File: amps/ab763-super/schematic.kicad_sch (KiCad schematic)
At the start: 122 parts, among them T1 125P5D · 360-0-360V, T2 125C1A, T3 125A9A, T4 125A20B

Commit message: Fix: AB763 Super PI tail, feedback 100, recovery grid leak, reservoir pair and valve sections, as the C-FD drawings show them
- PI tail: the 22K lands on the feedback node, with the 820 from the speaker,
  the .1-200 from the cold grid and a 100 to ground (schematic sh-001 at
  3299 x 2551, crop s-pifb). The sheet grounded the tail and had no 100.
  New RFB1 on the sheet and in the BOM. netlist.cir now has RT2 JPI NFB,
  RFB1 NFB 0 100 and RNFB NFB 0 820, as the Twin models it. The PI plates
  and tail re-simulate to 255.8 / 249.3 V and 97.5 / 95.5 V; the notes'
  table follows.
- Board: RT2 stands on the top row from the tail junction to node F, and RFB1
  from node F to ground; the layout letters '100' at the board's top edge.
  The speaker anchor names SPK.tip, so the 820 is DC-checked. The tremolo
  parts the board placed under the old sheet's names are renamed to the
  drawn ladder's CTO2, CTO3 and RTOG2. The 27K bias leg's declaration is
  renamed RINT -> RBIAS2. The filter-can scope rule now covers C10-C13, the
  series pair its reason already names.
- RGR1 220K is the recovery grid's leak to ground, and the tank output lands
  on the grid (crop s-recov). The sheet drew it in series. sch_map maps the
  netlist's RGRV to it.
- The reservoir is two 70-350 cans in series, C10 over the new C13, each with
  its own 220K 1W across it (crop s-reservoir). The sheet lumped one 70 uF
  with both 220K to ground.
- V6 and V5 sections: the layout page (3299 x 2551 copy) runs the 82K to
  pin 1 and the 100K to pin 6, and puts the oscillator on 1/2/3 (+280 V pin
  1, +2.5 V pin 3) and the lamp driver on 6/7/8 (+390 V pin 6, +17.0 V pin 8).
  V6A, V5A are unit 2; V6B, V5B unit 1.
- netlist.cir: the dry node GDRY is modelled (RGD1, CBD1, CCV2, CRS), as on
  the Twin.

Co-Authored-By: Claude Opus 5 (1M context) <noreply@anthropic.com>
Claude-Session: https://claude.ai/code/session_01KBMfdh37HmCL2iWcBiL5J1
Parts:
- removed CBIAS: 25u 50V, symbol cx:C
- removed CCD1: .1u, symbol cx:C
- removed RT2: 22k, symbol cx:R
- removed RTO10: 10M, symbol cx:R
- removed RTOG1: 1M, symbol cx:R
- removed V5A: 12AX7, symbol cx:TRIODE
- removed V6B: 12AT7, symbol cx:TRIODE
- added C13: 70u 350V, symbol cx:C
- added RBIAS2: 27k, symbol cx:R
- added RFB1: 100, symbol cx:R
- added RGPA, RTOG2: 1M, symbol cx:R
- added RLPA: 82k 5%, symbol cx:R
- added RMIXV: 220k, symbol cx:R
- added T1: 125P5D · 360-0-360V, symbol cx:PT
- added VRSPD: 3M-RA speed, symbol cx:POT
- C10: value 70u -> 70u 350V
- CBIAS: renamed from RBIAS2; value 27k -> 25u 50V; symbol cx:R -> cx:C
- CCD1: renamed from RMIXV; value 220k -> .1u; symbol cx:R -> cx:C
- CKTO1: renamed from VRSPD; value 3M-RA speed -> 25u; symbol cx:POT -> cx:C
- RLAMP: renamed from T1; value 125P5D · 360-0-360V -> 100k; symbol cx:PT -> cx:R
- RT2: renamed from RGPA; value 1M -> 22k
- RTO10: renamed from RLAMP; value 100k -> 10M
- V5A: renamed from CKTO1; value 25u -> 12AX7; symbol cx:C -> cx:TRIODE; Basing_unit (none) -> 2
- V5B: Basing_unit (none) -> 1
- V6A: Basing_unit (none) -> 2
- V6B: renamed from RLPA; value 82k 5% -> 12AT7; symbol cx:R -> cx:TRIODE; Basing_unit (none) -> 1
- renumbered RTOG2 to RTOG1
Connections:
- net BC: now also RLPA.1; no longer V6B.1
- net BIAS FILTER: now also CBIAS.1
- net BP1: now also RLAMP.2, RTO10.1; no longer RTO10.2
- net GND: now also CKTO1.2, RGR1.2, C13.2, RBIAS2.2, RFB1.2, T1.4 (HT_CT); no longer C10.2, RBL1.2, RLAMP.4 (HT_CT), V5A.2
- net HT_A: now also T1.3 (HT_A); no longer RLAMP.3 (HT_A)
- net HT_B: now also T1.5 (HT_B); no longer RLAMP.5 (HT_B)
- net MAINS: now also T1.1 (PRI_1); no longer RLAMP.1 (PRI_1)
- net MAINS N: now also T1.2 (PRI_2); no longer RLAMP.2 (PRI_2)
- net PIG: now also RMIXV.2; no longer CCD1.2
- net TANK RET: now also V3B.2 (G)
- net at VRBIAS.3: now also RBIAS2.1; no longer CBIAS.1
- net at C2.1, RLPB.2: now also V6B.1 (P)
- net at CPIA.2, V6A.2 (G): now also RGPA.1; no longer RT2.1
- net at RGPB.1, RTAIL.1: now also RT2.1, RGPA.2; no longer RT2.2
- net at RTAIL.2, V6A.3 (K): now also V6B.3 (K)
- net at VRINT.1: now also CCD1.2, RMIXV.1; no longer CCD1.1
- net at CTO1.1, RTO2.2: now also V5A.1 (P)
- net at C10.1, RBL1.1, T2.1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: no longer RBL2.1
- net at OPTO.2 (L2): now also RLAMP.1; no longer RTO10.1
- net at CTO1.2, CTO2.2: now also VRSPD.1, VRSPD.2 (W); no longer CKTO1.1, CKTO1.2 (W)
- net at RTO1.1: now also VRSPD.3; no longer CKTO1.3
- net at RKTO1.1: now also CKTO1.1, V5A.3 (K); no longer V5A.1
- net at OPTO.1 (L1), V5B.1 (P): now also RTO10.2
- net at CTO2.1, CTO3.1, V5B.2 (G): now also RTOG1.2
- net at CPIB.1, RNFB.2: now also RT2.2, RFB1.1
- net at RTOG1.1, RTOG3.1: now also RTOG2.1
- net at C1.1, V6A.1 (P): now also RLPA.2; no longer V6B.2
- net at CPIB.2, RGPB.2: now also V6B.2 (G)
- net at CTO3.2: now also V5A.2 (G), RTOG2.2; no longer RTOG1.2
- net at RLD1.2, V3A.1 (P): now also CCD1.1
- new net: C10.2, C13.1, RBL1.2, RBL2.1
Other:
- moved on the sheet: RT2, RTO10, RTOG1

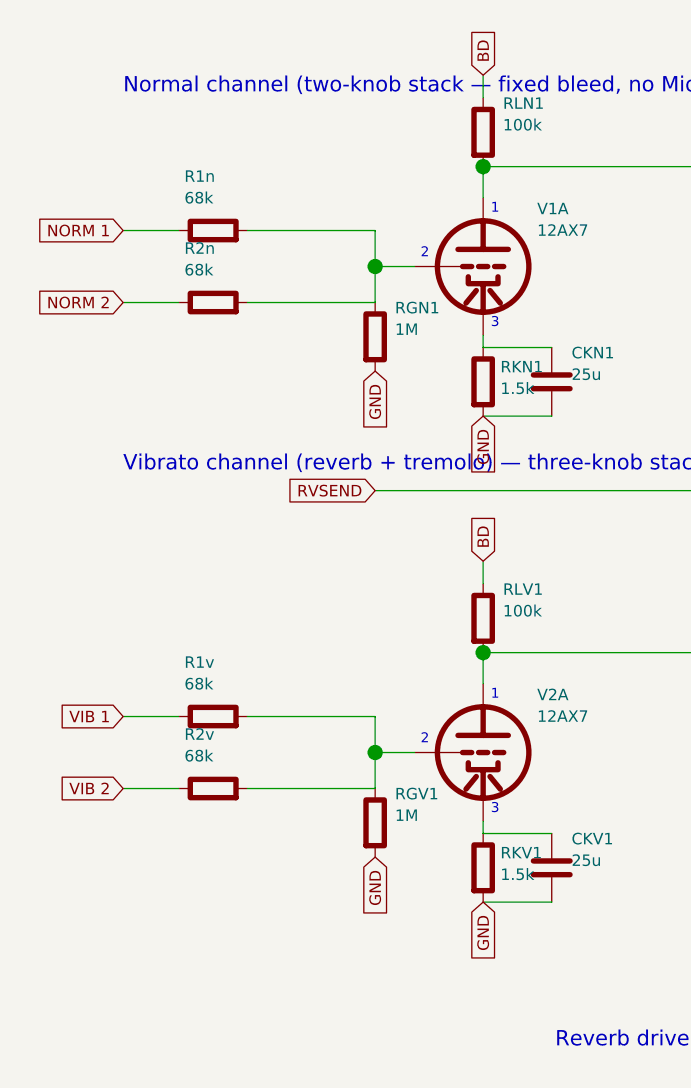
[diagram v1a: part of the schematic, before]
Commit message: AB763 Super (draft): input leaks at jack 1's tip (V1 audit carry-over)
The Super Reverb's own C-FD schematic (cached 2161x1500 capture, title
block 'SUPER-REVERB-AMP AB763', C-FD) hangs each channel's 1M from jack
1's tip, jack side of its lower 68k: Normal crop 90,250,300,500,
Vibrato 90,640,300,890. Jack 2's contact -> jack 1's tip, jack 1's
contact -> ground; the grid junction carries only the two 68ks. The
sheet had both leaks on the grid bus. Same fix as the Twin (1bab462)
and the Deluxe: R1n/R1v series_bridge, roles, jack note and circuit
story corrected. The board already mounts the leaks at the jacks
(net_map.netlist_unplaced). No DC node moves.

Co-Authored-By: Claude Opus 5.5 <noreply@anthropic.com>
Claude-Session: https://claude.ai/code/session_01KBMfdh37HmCL2iWcBiL5J1
Signed-off-by: AnalogMaker <theanalogmaker@gmail.com>
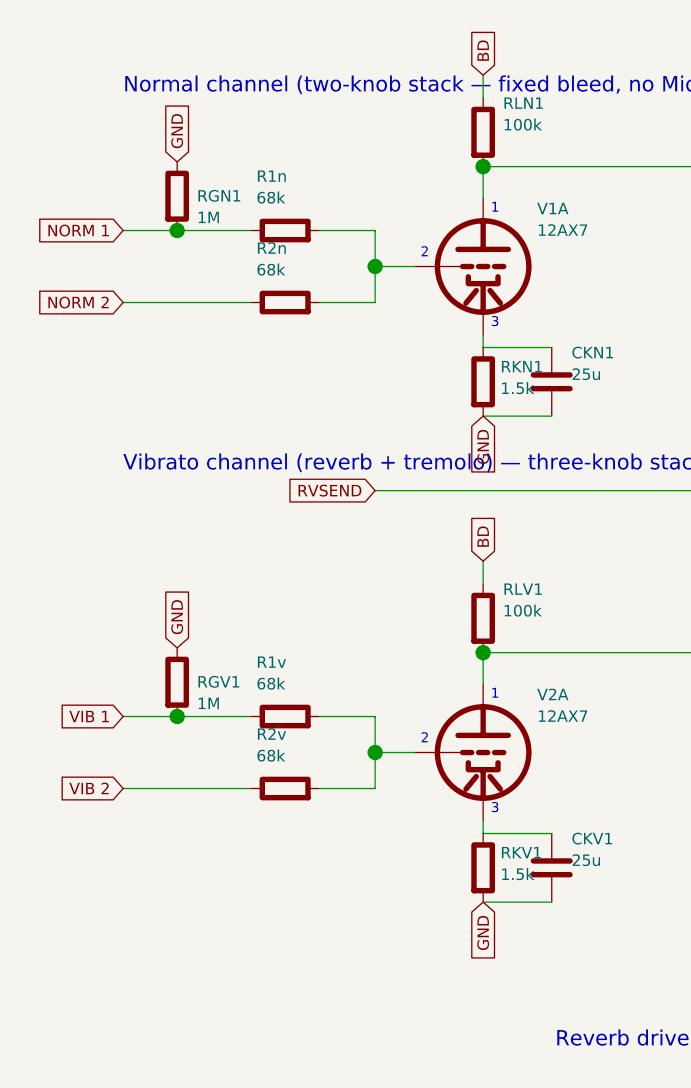
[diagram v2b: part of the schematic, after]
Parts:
- removed CBRN: 120p, symbol cx:C
- removed CBV: .1u, symbol cx:C
- removed CKRD, CKTO1, CKTO2: 25u, symbol cx:C
- removed CPIA: .001u, symbol cx:C
- removed CTO2: .01u, symbol cx:C
- removed CTV: 250p, symbol cx:C
- removed R2v: 68k, symbol cx:R
- removed RBL1: 220k 1W, symbol cx:R
- removed RLPA: 82k 5%, symbol cx:R
- removed RLR1, RLV1, RLV2: 100k, symbol cx:R
- removed RST1, RST2: 1.5k, symbol cx:R
- added C13: 70u 350V, symbol cx:C
- added RGV1, RTOG1: 1M, symbol cx:R
- added RKA, RKE: 820, symbol cx:R
- added RKV1: 1.5k, symbol cx:R
- added RLPB: 100k 5%, symbol cx:R
- added RS1, RS2: 470 1W, symbol cx:R
- added RTO10: 10M, symbol cx:R
- added SWBN: Bright, symbol cx:SWITCH
- added T4: 125A20B, symbol cx:OT_SE
- added V6B: 12AT7, symbol cx:TRIODE
- added VRBV: 250k-A bass, symbol cx:POT
- added VRSPD: 3M-RA speed, symbol cx:POT
- added VRTV: 250k-A treb, symbol cx:POT
- CBRN: renamed from SWBN; value Bright -> 120p; symbol cx:SWITCH -> cx:C
- CBV: renamed from VRBV; value 250k-A bass -> .1u; symbol cx:POT -> cx:C
- CKRD: renamed from T4; value 125A20B -> 25u; symbol cx:OT_SE -> cx:C
- CKTO1: renamed from CTO1; value .02u -> 25u
- CKTO2: renamed from RTO10; value 10M -> 25u; symbol cx:R -> cx:C
- CPIA: renamed from V6B; value 12AT7 -> .001u; symbol cx:TRIODE -> cx:C; Basing_unit 1 -> (none)
- CTO1: renamed from VRSPD; value 3M-RA speed -> .02u; symbol cx:POT -> cx:C
- CTO2: renamed from RTOG1; value 1M -> .01u; symbol cx:R -> cx:C
- CTV: renamed from VRTV; value 250k-A treb -> 250p; symbol cx:POT -> cx:C
- R2v: renamed from RGV1; value 1M -> 68k
- RBL1: renamed from C13; value 70u 350V -> 220k 1W; symbol cx:C -> cx:R
- RLPA: renamed from RLPB; value 100k 5% -> 82k 5%
- RLR1: renamed from RKE; value 820 -> 100k
- RLV1: renamed from RKV1; value 1.5k -> 100k
- RLV2: renamed from RKA; value 820 -> 100k
- RST1: renamed from RS1; value 470 1W -> 1.5k
- RST2: renamed from RS2; value 470 1W -> 1.5k
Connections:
- net BC: now also RLPB.1
- net BD: now also RLR1.1, RLV1.1, RLV2.1
- net BP1: now also RS1.2, RS2.2, RTO10.1; no longer CKTO2.1, RST1.2, RST2.2
- net GND: now also CKRD.2, CKTO1.2, CKTO2.2, RGN1.1, C13.2, RGV1.1, RKA.2, RKE.2, RKV1.2, T4.4 (SEC_C); no longer CKRD.4 (SEC_C), R2v.2, RBL1.2, RGN1.2, RLR1.2, RLV1.2, RLV2.2
- net KA: now also RKA.1; no longer RLV2.1
- net KE: now also RKE.1; no longer RLR1.1
- net NORM 1: now also RGN1.2
- net PIG: now also CPIA.1
- net REVERB TANK: now also T4.3 (SEC_H); no longer CKRD.3 (SEC_H)
- net VIB 1: now also RGV1.2
- net VIB 2: now also R2v.1
- net at C2.2, RGL2.1: now also RST2.1
- net at RTO2.2, V5A.1 (P): now also CTO1.1; no longer CKTO1.1
- net at RTOG2.1, RTOG3.1: now also RTOG1.1; no longer CTO2.1
- net at V8.2 (G1): now also RST2.2
- net at V8.3 (G2): now also RS2.1; no longer RST2.1
- net at VRTN.2 (W), VRVN.1: now also CBRN.1
- net at R1v.2, V2A.2 (G): now also R2v.2; no longer R2v.1
- net at RSV.1, V2A.1 (P): now also CTV.1, RLV1.2
- net at C10.1, T2.1, V9A.2 (K)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: now also RBL1.1
- net at RGPA.1, V6A.2 (G): now also CPIA.2
- net at CBV2.1, RSV.2: now also CBV.1
- net at OPTO.1 (L1), V5B.1 (P): now also RTO10.2; no longer CKTO2.2
- net at CKV1.1, V2A.3 (K): now also RKV1.1; no longer RLV1.1
- net at V1B.2 (G), VRVN.2 (W): now also SWBN.2; no longer CBRN.2
- net at RKTO1.1, V5A.3 (K): now also CKTO1.1
- net at CPIB.2, RGPB.2: now also V6B.2 (G); no longer CPIA.2 (G)
- net at RKRD.1, V4A.3 (K), V4B.3 (K): now also CKRD.1
- net at CCV2.1, V2B.1 (P): now also RLV2.2
- net at VRMV.1, VRMV.2 (W): now also VRBV.3; no longer CBV.3
- net at C1.1, V6A.1 (P): now also RLPA.2
- net at RTAIL.2, V6A.3 (K): now also V6B.3 (K); no longer CPIA.3 (K)
- net at RST1.1: now also C1.2, RGL1.2; no longer V7.3 (G2)
- net at V7.2 (G1): now also RST1.2
- net at CBRV.1, VRVV.1: now also VRTV.2 (W); no longer CTV.2 (W)
- net at C10.2, RBL2.1: now also RBL1.2, C13.1; no longer RBL1.1
- net at CTO3.1, V5B.2 (G): now also CTO2.1, RTOG1.2; no longer CTO2.2
- net at RKTO2.1, V5B.3 (K): now also CKTO2.1
- net at R1n.2, R2n.2, V1A.2 (G): no longer RGN1.1
- net at CCR1.1, V3B.1 (P): now also RLR1.2
- net at RTO1.1: now also VRSPD.3; no longer CTO1.3
- new net: C2.1, RLPB.2, V6B.1 (P)
- new net: VRBV.1, VRBV.2 (W), VRTV.3
- new net: CTO1.2, CTO2.2, VRSPD.1, VRSPD.2 (W)
- new net: CTV.2, VRTV.1
- new net: RS1.1, V7.3 (G2)
- new net: CBRN.2, SWBN.1
- now unconnected: CBV.2 (W)
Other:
- moved on the sheet: CKTO1, R1n, R2v, RLPA, RLR1, RLV1, RLV2, RST1, RST2
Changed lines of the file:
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@@
   (global_label "NORM 2" (shape input) (at 19.6088 43.889 180)
     (effects (font (size 1.27 1.27)) (justify right)))
-  (symbol (lib_id "cx:R") (at 29.6088 35.889 90) (unit 1)
-    (in_bom yes) (on_board yes)
-    (property "Reference" "R1n" (at 26.4088 29.889 270) (effects (font (size 1.27 1.27)) (justify left)))
-    (property "Value" "68k" (at 26.4088 32.289 270) (effects (font (size 1.27 1.27)) (justify left))))
-  (wire (pts (xy 19.6088 35.889) (xy 25.7988 35.889))
-    (stroke (width 0) (type default)))
-  (wire (pts (xy 33.4188 35.889) (xy 47.6088 35.889))
-    (stroke (width 0) (type default)))
-  (symbol (lib_id "cx:R") (at 29.6088 43.889 90) (unit 1)
-    (in_bom yes) (on_board yes)
-    (property "Reference" "R2n" (at 26.4088 37.889 270) (effects (font (size 1.27 1.27)) (justify left)))
-    (property "Value" "68k" (at 26.4088 40.289 270) (effects (font (size 1.27 1.27)) (justify left))))
-  (wire (pts (xy 19.6088 43.889) (xy 25.7988 43.889))
-    (stroke (width 0) (type default)))
-  (wire (pts (xy 33.4188 43.889) (xy 47.6088 43.889))
+  (symbol (lib_id "cx:R") (at 37.6088 35.889 90) (unit 1)
+    (in_bom yes) (on_board yes)
+    (property "Reference" "R1n" (at 34.4088 29.889 270) (effects (font (size 1.27 1.27)) (justify left)))
+    (property "Value" "68k" (at 34.4088 32.289 270) (effects (font (size 1.27 1.27)) (justify left))))
+  (wire (pts (xy 19.6088 35.889) (xy 25.6088 35.889))
+    (stroke (width 0) (type default)))
+  (wire (pts (xy 25.6088 35.889) (xy 33.7988 35.889))
+    (stroke (width 0) (type default)))
+  (wire (pts (xy 41.4188 35.889) (xy 47.6088 35.889))
+    (stroke (width 0) (type default)))
+  (junction (at 25.6088 35.889) (diameter 1.7) (color 0 0 0 0))
+  (symbol (lib_id "cx:R") (at 25.6088 32.079 0) (unit 1)
+    (in_bom yes) (on_board yes)
+    (property "Reference" "RGN1" (at 27.8088 32.079 0) (effects (font (size 1.27 1.27)) (justify left)))
+    (property "Value" "1M" (at 27.8088 34.479 0) (effects (font (size 1.27 1.27)) (justify left))))
+  (global_label "GND" (shape input) (at 25.6088 28.269 90)
+    (effects (font (size 1.27 1.27)) (justify left)))
+  (symbol (lib_id "cx:R") (at 37.6088 43.889 90) (unit 1)
+    (in_bom yes) (on_board yes)
+    (property "Reference" "R2n" (at 34.4088 37.889 270) (effects (font (size 1.27 1.27)) (justify left)))
+    (property "Value" "68k" (at 34.4088 40.289 270) (effects (font (size 1.27 1.27)) (justify left))))
+  (wire (pts (xy 19.6088 43.889) (xy 33.7988 43.889))
+    (stroke (width 0) (type default)))
+  (wire (pts (xy 41.4188 43.889) (xy 47.6088 43.889))
     (stroke (width 0) (type default)))
   (wire (pts (xy 47.6088 35.889) (xy 47.6088 39.889))
@@
     (stroke (width 0) (type default)))
   (junction (at 47.6088 39.889) (diameter 1.7) (color 0 0 0 0))
-  (symbol (lib_id "cx:R") (at 47.6088 47.699 0) (unit 1)
-    (in_bom yes) (on_board yes)
-    (property "Reference" "RGN1" (at 49.8088 44.499 0) (effects (font (size 1.27 1.27)) (justify left)))
-    (property "Value" "1M" (at 49.8088 46.899 0) (effects (font (size 1.27 1.27)) (justify left))))
-  (global_label "GND" (shape input) (at 47.6088 51.509 270)
-    (effects (font (size 1.27 1.27)) (justify right)))
   (symbol (lib_id "cx:TRIODE") (at 59.6088 39.889 0) (unit 1)
     (in_bom yes) (on_board yes)
@@
   (global_label "VIB 2" (shape input) (at 19.6088 97.889 180)
     (effects (font (size 1.27 1.27)) (justify right)))
-  (symbol (lib_id "cx:R") (at 29.6088 89.889 90) (unit 1)
-    (in_bom yes) (on_board yes)
-    (property "Reference" "R1v" (at 26.4088 83.889 270) (effects (font (size 1.27 1.27)) (justify left)))
-    (property "Value" "68k" (at 26.4088 86.289 270) (effects (font (size 1.27 1.27)) (justify left))))
-  (wire (pts (xy 19.6088 89.889) (xy 25.7988 89.889))
-    (stroke (width 0) (type default)))
-  (wire (pts (xy 33.4188 89.889) (xy 47.6088 89.889))
-    (stroke (width 0) (type default)))
-  (symbol (lib_id "cx:R") (at 29.6088 97.889 90) (unit 1)
-    (in_bom yes) (on_board yes)
-    (property "Reference" "R2v" (at 26.4088 91.889 270) (effects (font (size 1.27 1.27)) (justify left)))
-    (property "Value" "68k" (at 26.4088 94.289 270) (effects (font (size 1.27 1.27)) (justify left))))
-  (wire (pts (xy 19.6088 97.889) (xy 25.7988 97.889))
-    (stroke (width 0) (type default)))
-  (wire (pts (xy 33.4188 97.889) (xy 47.6088 97.889))
+  (symbol (lib_id "cx:R") (at 37.6088 89.889 90) (unit 1)
+    (in_bom yes) (on_board yes)
+    (property "Reference" "R1v" (at 34.4088 83.889 270) (effects (font (size 1.27 1.27)) (justify left)))
+    (property "Value" "68k" (at 34.4088 86.289 270) (effects (font (size 1.27 1.27)) (justify left))))
+  (wire (pts (xy 19.6088 89.889) (xy 25.6088 89.889))
+    (stroke (width 0) (type default)))
+  (wire (pts (xy 25.6088 89.889) (xy 33.7988 89.889))
+    (stroke (width 0) (type default)))
+  (wire (pts (xy 41.4188 89.889) (xy 47.6088 89.889))
+    (stroke (width 0) (type default)))
+  (junction (at 25.6088 89.889) (diameter 1.7) (color 0 0 0 0))
+  (symbol (lib_id "cx:R") (at 25.6088 86.079 0) (unit 1)
+    (in_bom yes) (on_board yes)
+    (property "Reference" "RGV1" (at 27.8088 86.079 0) (effects (font (size 1.27 1.27)) (justify left)))
+    (property "Value" "1M" (at 27.8088 88.479 0) (effects (font (size 1.27 1.27)) (justify left))))
+  (global_label "GND" (shape input) (at 25.6088 82.269 90)
+    (effects (font (size 1.27 1.27)) (justify left)))
+  (symbol (lib_id "cx:R") (at 37.6088 97.889 90) (unit 1)
+    (in_bom yes) (on_board yes)
+    (property "Reference" "R2v" (at 34.4088 91.889 270) (effects (font (size 1.27 1.27)) (justify left)))
+    (property "Value" "68k" (at 34.4088 94.289 270) (effects (font (size 1.27 1.27)) (justify left))))
+  (wire (pts (xy 19.6088 97.889) (xy 33.7988 97.889))
+    (stroke (width 0) (type default)))
+  (wire (pts (xy 41.4188 97.889) (xy 47.6088 97.889))
     (stroke (width 0) (type default)))
   (wire (pts (xy 47.6088 89.889) (xy 47.6088 93.889))
@@
     (stroke (width 0) (type default)))
   (junction (at 47.6088 93.889) (diameter 1.7) (color 0 0 0 0))
-  (symbol (lib_id "cx:R") (at 47.6088 101.699 0) (unit 1)
-    (in_bom yes) (on_board yes)
-    (property "Reference" "RGV1" (at 49.8088 98.499 0) (effects (font (size 1.27 1.27)) (justify left)))
-    (property "Value" "1M" (at 49.8088 100.899 0) (effects (font (size 1.27 1.27)) (justify left))))
-  (global_label "GND" (shape input) (at 47.6088 105.509 270)
-    (effects (font (size 1.27 1.27)) (justify right)))
   (symbol (lib_id "cx:TRIODE") (at 59.6088 93.889 0) (unit 1)
     (in_bom yes) (on_board yes)
